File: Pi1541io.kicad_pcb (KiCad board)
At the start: 2 copper layers, 65 x 56 mm, 30 parts, among them J1 IEC1, J2 IEC2, J3 IEC3, J4 ExtSpkr, J5 GS3, J6 GS3, J7 GS3, J8 GS3, P1 Conn_02x20_Odd_Even, SW1 SW_Push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

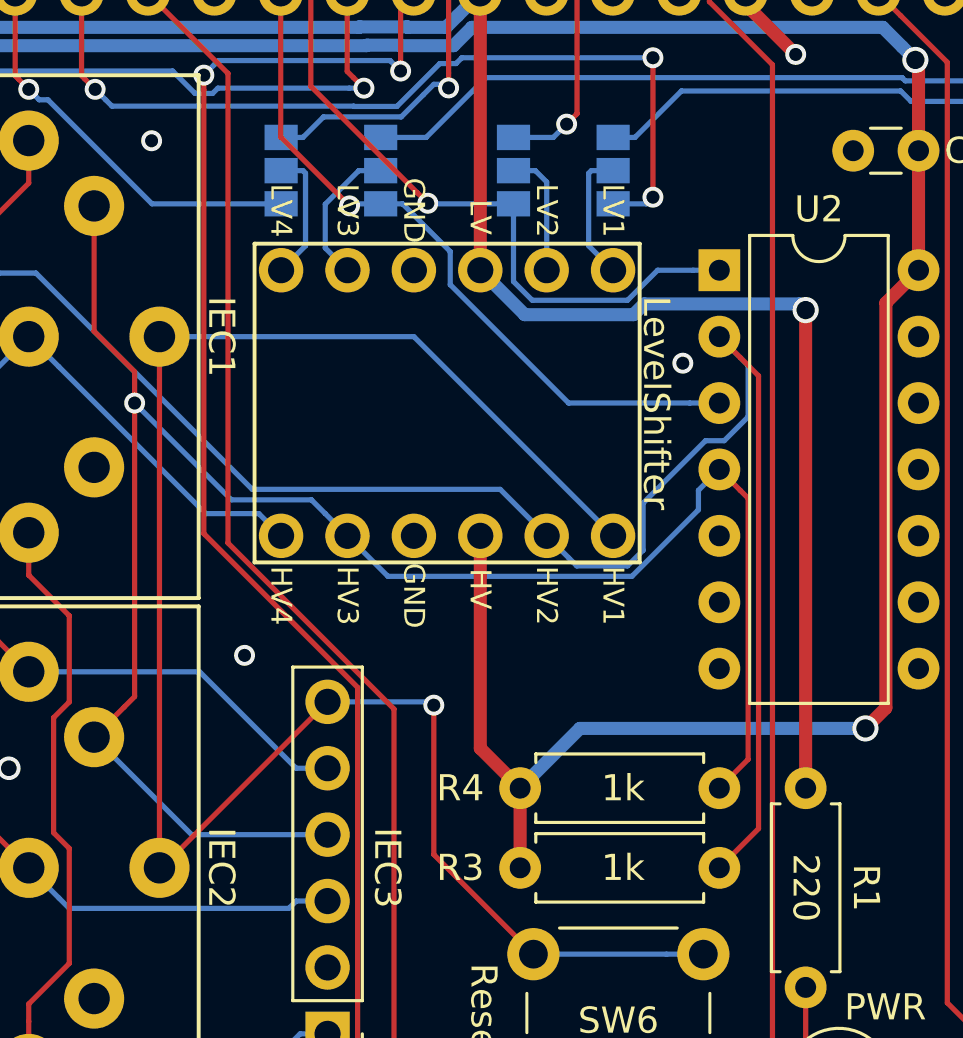
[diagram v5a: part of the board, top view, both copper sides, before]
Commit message: Discrete components to optionally replace the level shifter module.
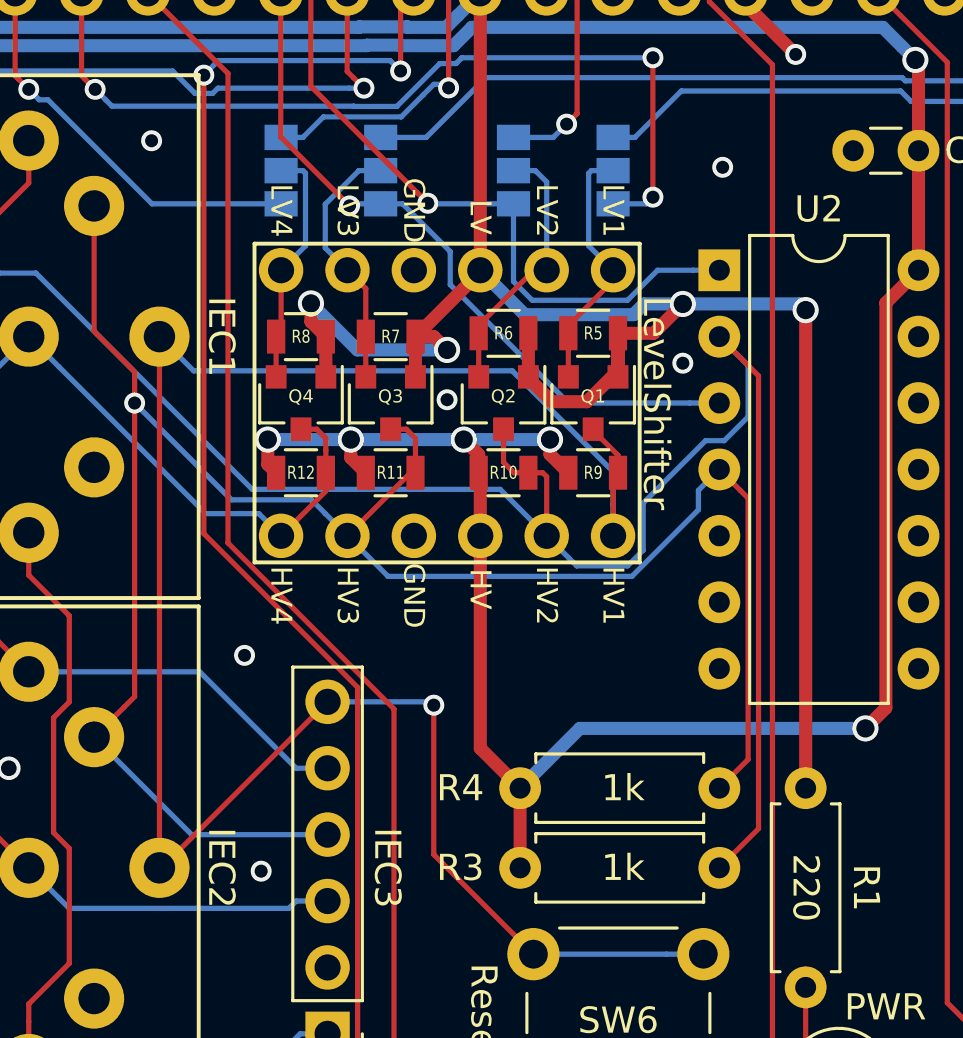
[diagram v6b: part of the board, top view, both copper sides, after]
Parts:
- added Q1: BSS138, TO_SOT_Packages_SMD:SOT-23, F.Cu at (139.2, 79.6)
- added Q2: BSS138, TO_SOT_Packages_SMD:SOT-23, F.Cu at (135.7, 79.6)
- added Q3: BSS138, TO_SOT_Packages_SMD:SOT-23, F.Cu at (131.4, 79.6)
- added Q4: BSS138, TO_SOT_Packages_SMD:SOT-23, F.Cu at (128.0, 79.6)
- added R10: R, Resistors_SMD:R_0805, F.Cu at (135.7, 82.3)
- added R11: R, Resistors_SMD:R_0805, F.Cu at (131.4, 82.3)
- added R12: R, Resistors_SMD:R_0805, F.Cu at (128.0, 82.3)
- added R5: R, Resistors_SMD:R_0805, F.Cu at (139.2, 77.0)
- added R6: R, Resistors_SMD:R_0805, F.Cu at (135.7, 77.0)
- added R7: R, Resistors_SMD:R_0805, F.Cu at (131.4, 77.1)
- added R8: R, Resistors_SMD:R_0805, F.Cu at (128.0, 77.1)
- added R9: R, Resistors_SMD:R_0805, F.Cu at (139.2, 82.3)
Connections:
- net Net-(J5-Pad2) renamed RESET_3V
- net Net-(J6-Pad2) renamed DATA_3V
- net Net-(J7-Pad2) renamed CLK_3V
- net Net-(J8-Pad2) renamed ATN_3V
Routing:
- net +3V3: track 63.7 -> 91.3 mm, vias 1 -> 4
- net +5V: track 100.2 -> 119.4 mm, vias 2 -> 6
- net CLK: track 72.4 -> 78.4 mm
- net RESET: track 71.6 -> 77.6 mm
- net ATN: track 47.6 -> 53.2 mm
- net DATA_3V: track 4.83 -> 10.3 mm
- net DATA: track 96.9 -> 102.3 mm
- net RESET_3V: track 5.07 -> 9.86 mm
- net CLK_3V: track 5.53 -> 9.90 mm
- net ATN_3V: track 5.07 -> 9.23 mm
- net GND: vias 6 -> 9

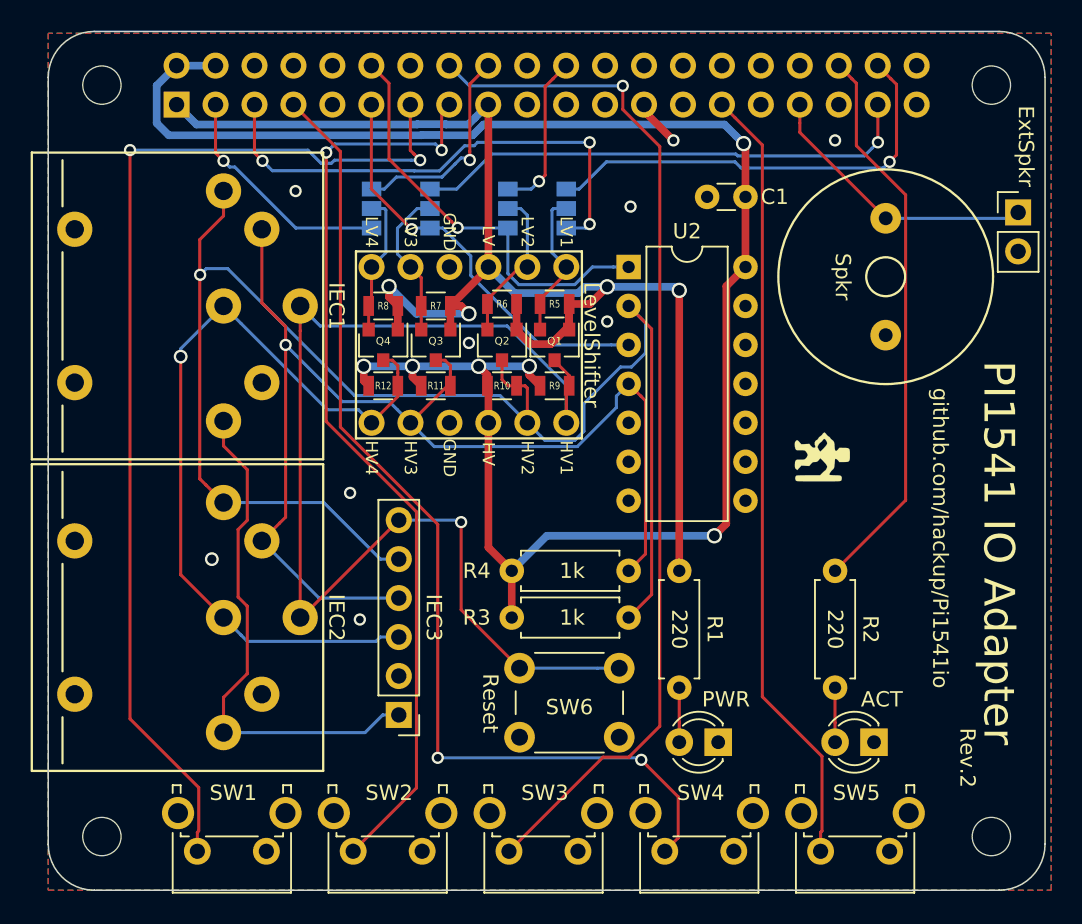
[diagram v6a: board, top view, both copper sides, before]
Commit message: Added optional components for reserved SRQ pins.
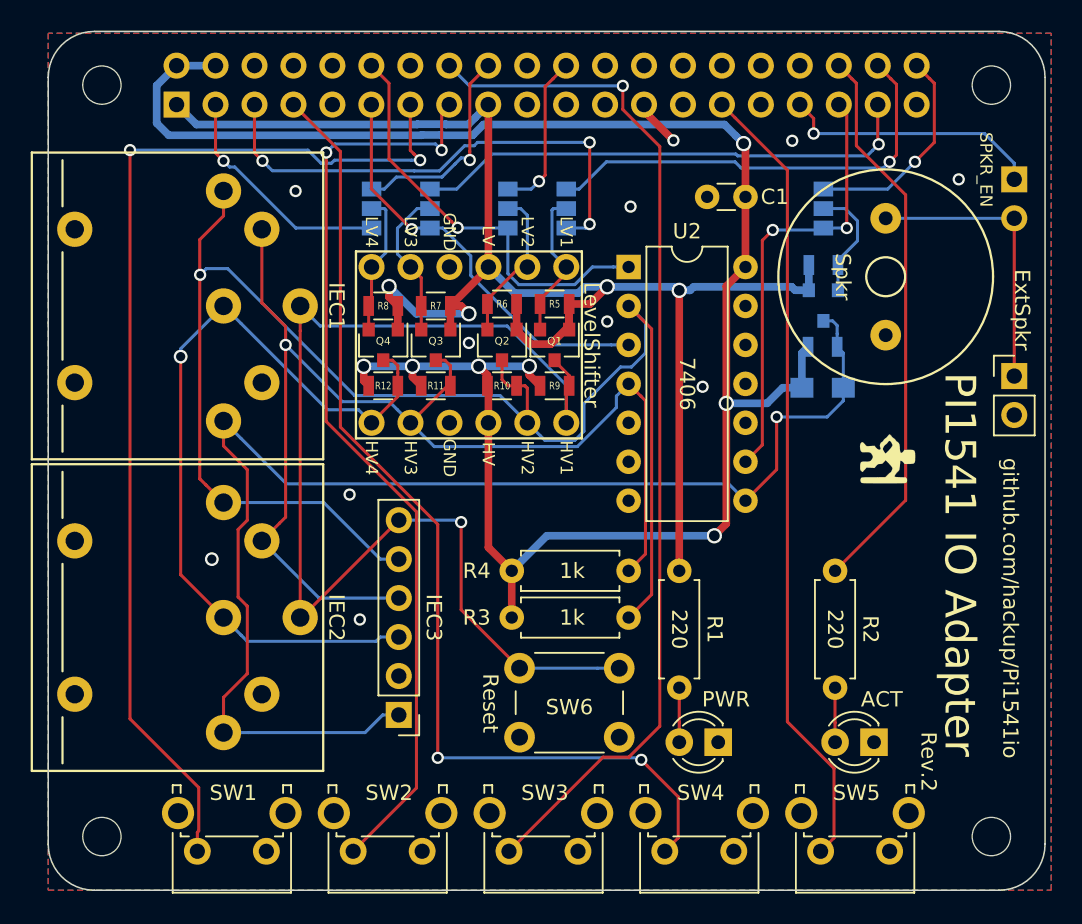
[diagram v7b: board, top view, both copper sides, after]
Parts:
- added J9: GS3, Connectors:GS3, B.Cu at (156.7, 70.8)
- added JP1: SPKR_EN, Pin_Headers:Pin_Header_Straight_1x02_Pitch2.54mm, F.Cu at (169.1, 68.8)
- added Q5: BSS138, TO_SOT_Packages_SMD:SOT-23, B.Cu at (156.7, 77.1)
- added R13: 1k, Resistors_SMD:R_0805_HandSoldering, B.Cu at (156.6, 82.4)
- added R14: R, Resistors_SMD:R_0805, B.Cu at (156.7, 74.4)
- added R15: R, Resistors_SMD:R_0805, B.Cu at (156.6, 79.8)
- moved J4 10.7 mm to (169.1, 81.7)
- moved G*** 4.26 mm to (160.9, 87.1)
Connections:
- J4 pad 1: /GPIO13(PWM1) -> Net-(J4-Pad1)
- LS1 pad 1: /GPIO13(PWM1) -> Net-(J4-Pad1)
- P1 pad 40: /GPIO21(SPI1_SCK) -> SRQ_IN
- U2 pad 8: (no net) -> SRQ
- U2 pad 9: (no net) -> SRQ_BD
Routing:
- net SRQ: track 34.0 -> 87.4 mm, vias 0 -> 1
- net SRQ_BD: track 0.00 -> 29.0 mm, vias 0 -> 2
- net Net-(J4-Pad1): track 0.00 -> 18.7 mm
- net SRQ_IN: track 0.00 -> 14.0 mm, vias 0 -> 1
- net +3V3: track 91.3 -> 101.6 mm
- net +5V: track 119.4 -> 127.6 mm, vias 6 -> 7
- net SRQ_3V: track 0.00 -> 7.60 mm
- net /GPIO13(PWM1): track 18.5 -> 17.2 mm, vias 0 -> 1
- net /GPIO5: track 51.4 -> 52.1 mm
- net GND: vias 9 -> 11
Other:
- board text added: "SRQ reserved"

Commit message: Project spelling.
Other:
- board text added: "Pi1541 IO Adapter"
- board text removed: "PI1541 IO Adapter"
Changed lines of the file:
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@@
   (page A4)
   (title_block
-    (title "PI1541 IO Adapter")
+    (title "Pi1541 IO Adapter")
     (date 2018-05-25)
     (rev 2)
@@
     (effects (font (size 1 1) (thickness 0.2)) (justify left))
   )
-  (gr_text "PI1541 IO Adapter" (at 165.583 81.42 270) (layer F.SilkS)
+  (gr_text "Pi1541 IO Adapter" (at 165.583 81.42 270) (layer F.SilkS)
     (effects (font (size 2 2) (thickness 0.3)) (justify left))
   )
